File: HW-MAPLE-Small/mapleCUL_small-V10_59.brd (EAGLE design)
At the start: 80 x 30 mm, 18 parts, among them IC2 LAN-USR-ES1

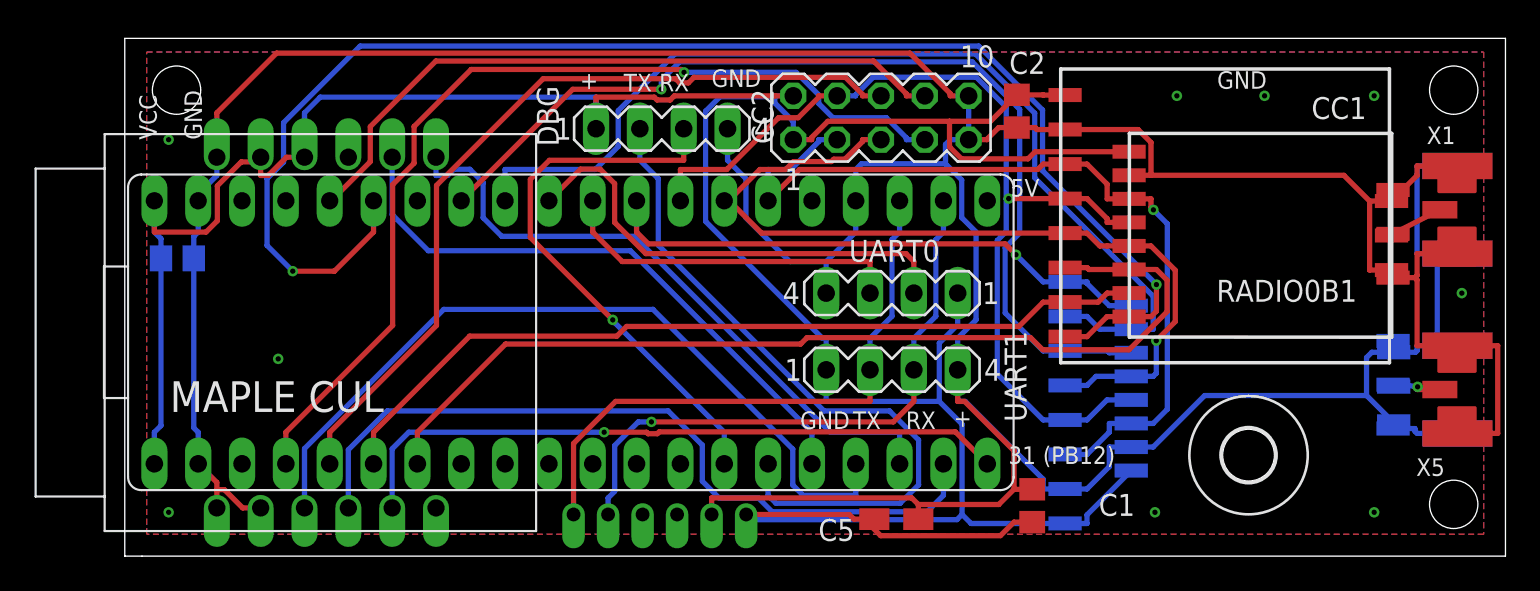
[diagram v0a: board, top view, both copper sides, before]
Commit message: Update RFM95, etc.
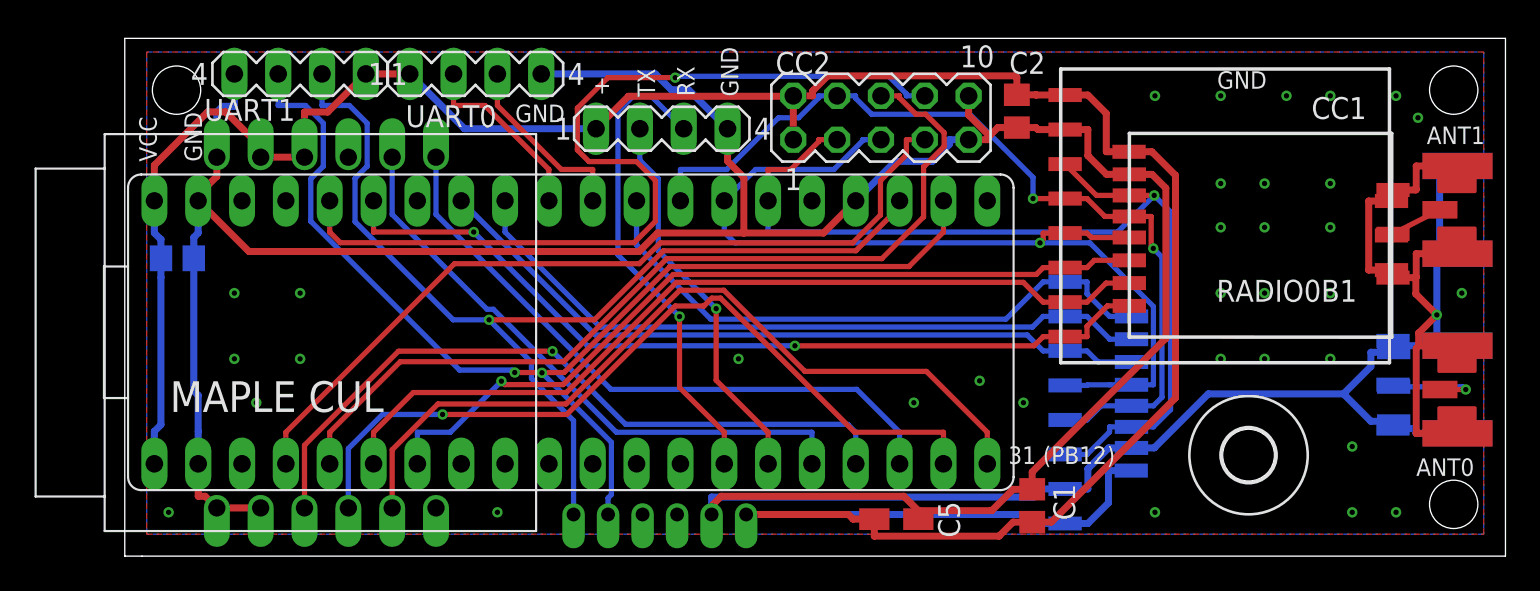
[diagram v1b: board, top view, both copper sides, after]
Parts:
- RADIO0B1: value CC1101_MODULE1SMALL -> CC1101_MODULE1SMD
- moved UART1 38.3 mm to (10.2, 27.9), turned to 180 degrees
- moved UART0 27.3 mm to (20.3, 27.9), turned to 0 degrees
- renumbered X1 to ANT1, X5 to ANT0
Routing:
- net CC_CS1: track 84.7 -> 49.6 mm
- net RX1: track 34.9 -> 66.3 mm, vias 1 -> 2
- net TX1: track 34.6 -> 61.1 mm, vias 0 -> 1
- net VCC: track 185.7 -> 159.7 mm
- net TX_DBG: track 40.7 -> 22.5 mm, vias 0 -> 1
- net CC_OUT_0: track 58.7 -> 41.2 mm
- net TX-MAPLE: track 27.3 -> 10.7 mm
- net CC_IN_0: track 57.5 -> 42.7 mm, vias 1 -> 0
- net CC_OUT_2: track 39.9 -> 52.9 mm, vias 0 -> 1
- net RX-MAPLE: track 20.4 -> 10.7 mm
- net GND: track 268.1 -> 258.4 mm, vias 9 -> 35
- net CC_IN_1: track 56.8 -> 47.4 mm, vias 0 -> 1
- net CC_CS2: track 55.6 -> 47.5 mm, vias 1 -> 0
- net WIZ_CS: track 39.2 -> 46.9 mm, vias 1 -> 0
- net MOSI1: track 50.9 -> 57.7 mm
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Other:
- board text added: "Small V1.0 www.neuby.de"
- board text removed: "5V"
- board text removed: "V0.2 www.neuby.de"
